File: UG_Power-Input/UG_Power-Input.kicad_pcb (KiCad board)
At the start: 2 copper layers, 45 parts, among them J1 INPUT, J2 OUTPUT, J3 OUTPUT, U1 LM2679

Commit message: Changes to PCB design
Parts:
- added R3: 0Ω, Resistor_THT:R_Axial_DIN0207_L6.3mm_D2.5mm_P10.16mm_Horizontal, F.Cu at (106.9, 109.0)
- H3: footprint MountingHole:MountingHole_3.5mm -> MountingHole:MountingHole_3.5mm_Pad_Via
- R1: value 100kΩ 1% -> 100kΩ
- R2: value 4.99kΩ 1% -> 4.99kΩ; footprint Resistor_THT:R_Axial_DIN0207_L6.3mm_D2.5mm_P2.54mm_Vertical -> Resistor_THT:R_Axial_DIN0207_L6.3mm_D2.5mm_P10.16mm_Horizontal
- moved TP11 65.8 mm to (199.4, 65.3)
- moved F2 65.3 mm to (168.4, 123.7)
- moved TP6 65.0 mm to (181.1, 109.5), turned to 90 degrees
- moved R2 64.5 mm to (190.8, 113.3)
- moved R1 64.5 mm to (172.5, 105.7)
- moved C1 64.5 mm to (167.6, 83.3)
- moved TP10 64.2 mm to (202.7, 86.4)
- moved U1 64.2 mm to (196.1, 108.2)
- moved L1 64.1 mm to (140.7, 79.8)
- moved L3 64.1 mm to (140.7, 113.8)
- moved C7 64.1 mm to (193.3, 108.2)
- moved C9 64.1 mm to (201.2, 105.2)
- moved D1 64.1 mm to (195.6, 103.6)
- moved F1 64.1 mm to (178.3, 69.8)
- moved FL1 64.1 mm to (119.1, 84.3)
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- renumbered TP11 to TP10, TP10 to TP11
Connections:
- net Net-(FL1-Pad2) renamed -IN
- H3 pad 1: (no net) -> Net-(H3-Pad1)
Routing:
- net Net-(H3-Pad1): track 0.00 -> 6.55 mm
- net GND: vias 6 -> 12
- added copper zone on F.Cu, net GND

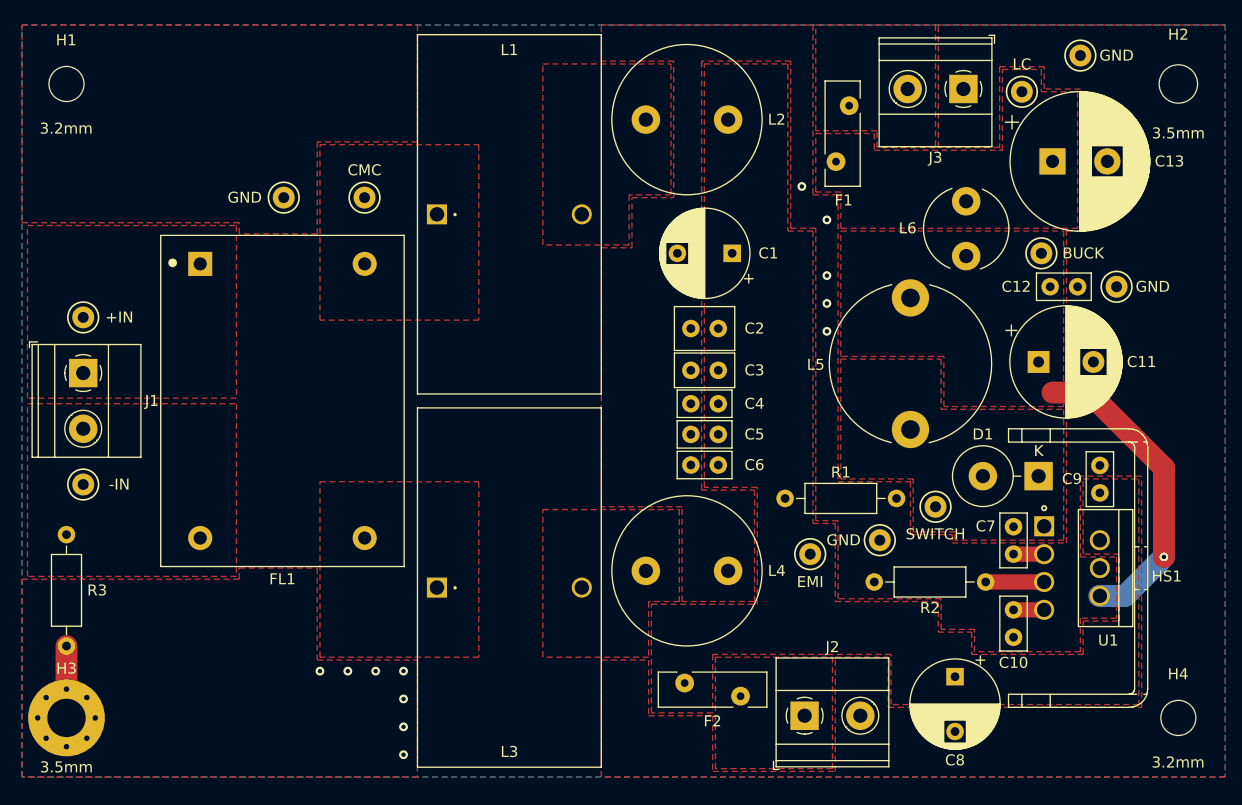
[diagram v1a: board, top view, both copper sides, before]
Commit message: Changes to silkscreen on back of PCB
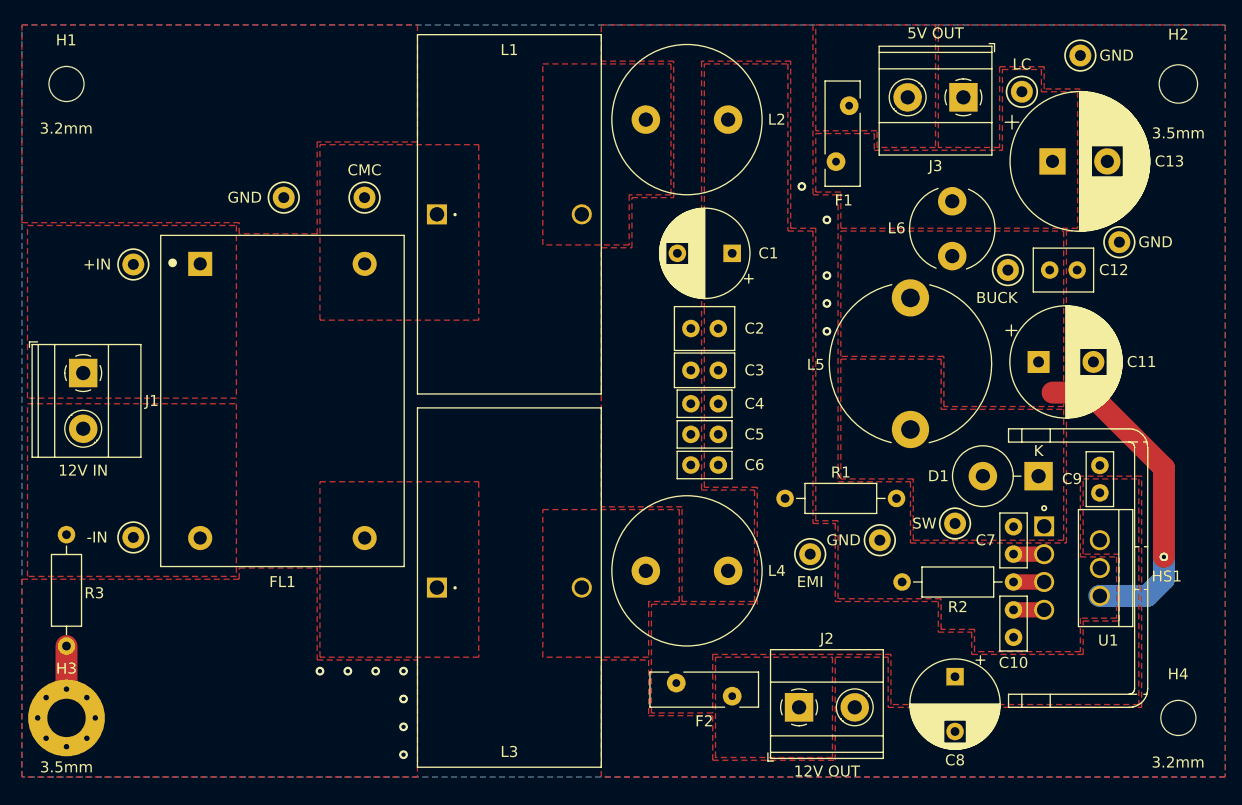
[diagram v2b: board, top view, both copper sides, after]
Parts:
- C12: footprint Capacitor_THT:C_MLCC_W5.0mm_L2.5mm_P2.50mm -> Capacitor_THT:C_MLCC_W5.5mm_L4.0mm_P2.50mm
- J1: value INPUT -> 12V IN
- J2: value OUTPUT -> 12V OUT
- J3: value OUTPUT -> 5V OUT
- TP9: value SWITCH -> SW
- moved TP1 6.65 mm to (113.0, 84.3)
- moved TP4 6.65 mm to (113.0, 109.2)
- moved TP10 4.07 mm to (202.9, 82.3)
- moved TP7 3.41 mm to (192.8, 84.8)
- moved R2 2.54 mm to (193.3, 113.3)
- moved TP9 2.34 mm to (188.0, 108.0)
- moved C12 1.52 mm to (196.6, 84.8)
- moved L6 1.27 mm to (187.7, 83.6)
- moved J2 0.92 mm to (173.7, 124.7)
- moved F2 0.76 mm to (167.6, 123.7)
- moved J3 0.76 mm to (188.7, 69.1)
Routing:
- net Net-(R2-Pad1): track 5.33 -> 2.79 mm
- net BUCK.OUT: track 28.5 -> 29.7 mm

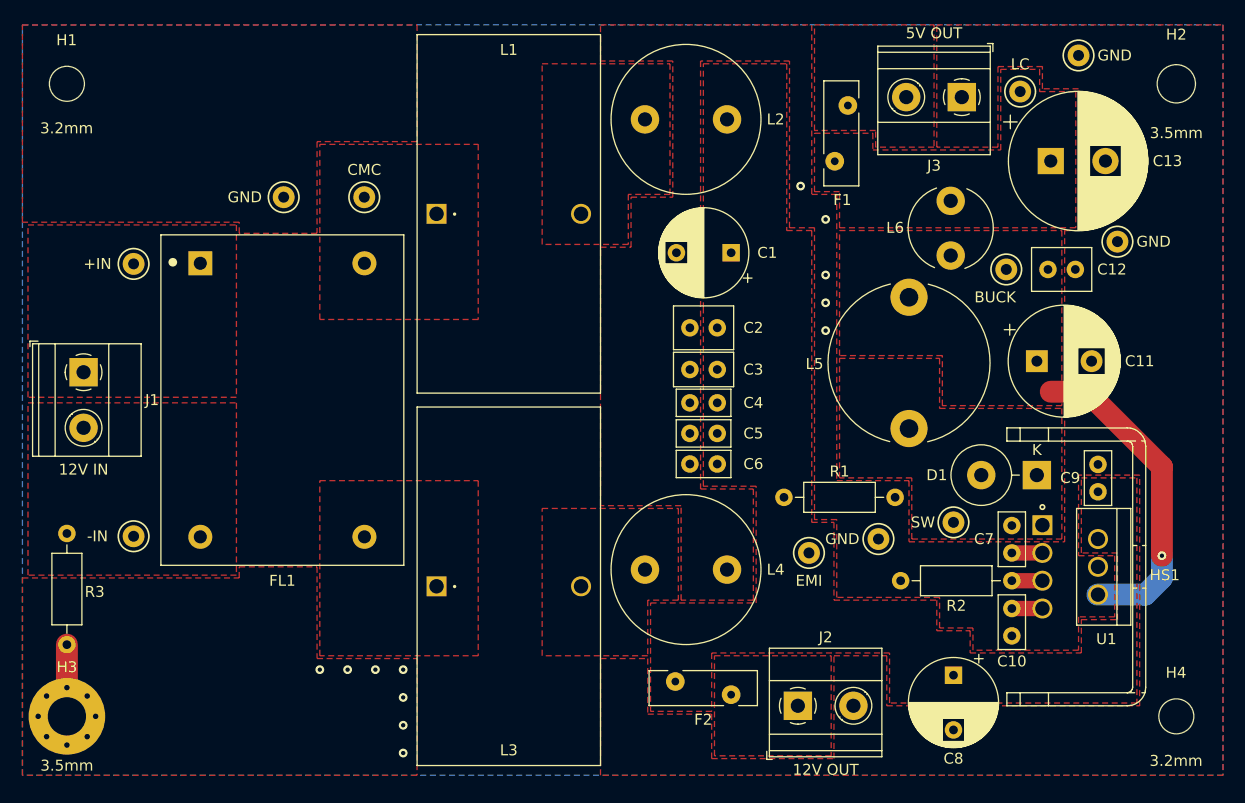
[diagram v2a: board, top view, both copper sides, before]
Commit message: Changes to schematic values, footprints on PCB, BOM
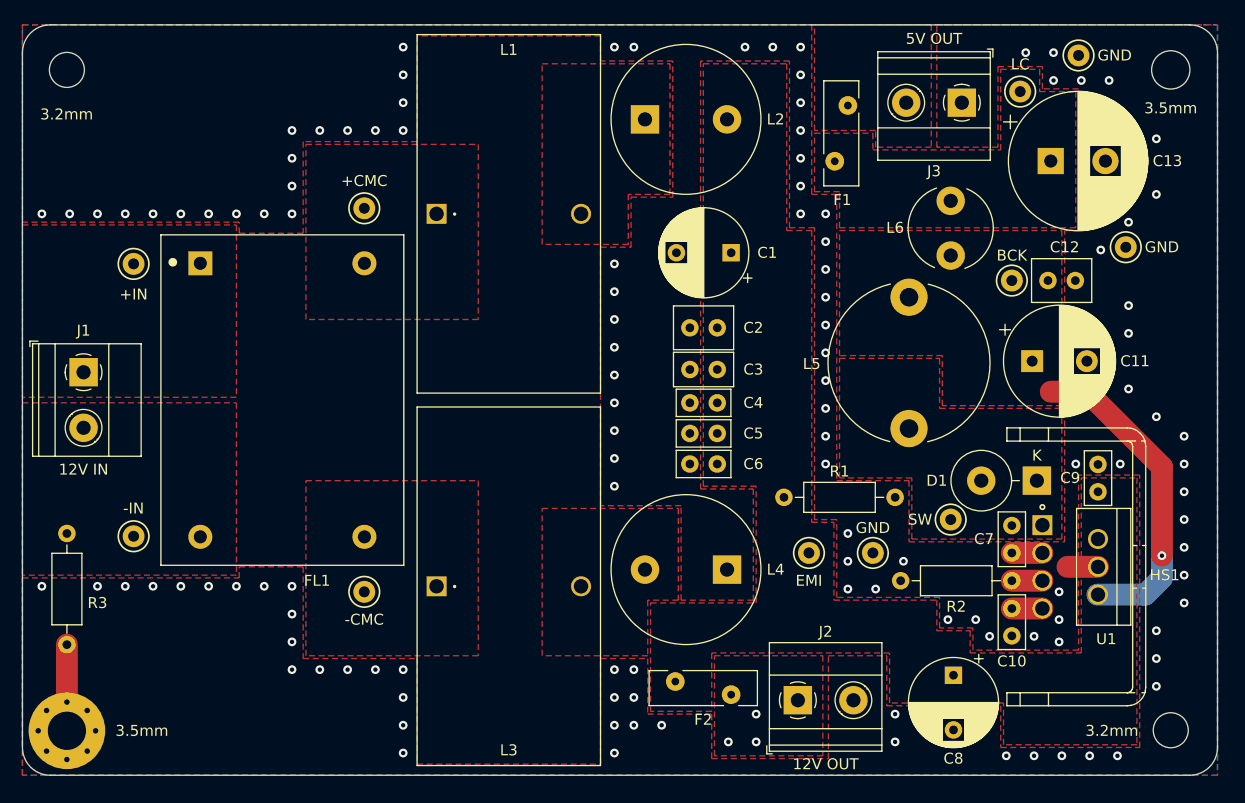
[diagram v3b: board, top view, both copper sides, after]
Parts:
- L5: value 10µH 10A -> 10µH 11.4A
- TP2: value CMC -> +CMC
- TP5: value GND -> -CMC
- TP7: value BUCK -> BCK
- moved TP5 36.8 mm to (134.1, 114.3)
- moved TP6 1.37 mm to (180.6, 110.7)
- moved H2 1.37 mm to (207.8, 66.6)
- moved H4 1.37 mm to (207.8, 126.9)
- moved H3 1.32 mm to (106.9, 127.0)
- moved H1 1.27 mm to (106.9, 66.6)
- moved TP7 1.14 mm to (193.3, 85.9)
- moved C12 1.02 mm to (196.6, 85.9)
- moved TP2 1.02 mm to (134.1, 79.2)
- moved TP10 0.92 mm to (203.7, 82.8)
- moved J3 0.51 mm to (188.7, 69.6)
- moved D1 0.51 mm to (195.6, 104.1)
- moved J2 0.51 mm to (173.7, 124.2)
- moved C11 0.43 mm to (195.2, 93.2)
- moved TP9 0.36 mm to (187.7, 107.7)
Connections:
- TP5 pad 1: GND -> Net-(FL1-Pad3)
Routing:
- net GND: track 0.00 -> 2.79 mm, vias 12 -> 124
- net Net-(H3-Pad1): track 6.55 -> 7.82 mm
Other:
- board outline added: 109.2 x 68.6 mm

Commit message: Changes to PCB & BOM
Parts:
- moved F1 12.0 mm to (190.2, 70.6)
- moved L6 5.33 mm to (182.4, 83.6)
- moved J3 5.08 mm to (183.6, 69.6)
- moved TP7 0.25 mm to (193.0, 85.9)
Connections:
- J3 pad 1: GND -> Net-(F1-Pad1)
- J3 pad 2: Net-(F1-Pad1) -> GND
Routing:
- net GND: vias 124 -> 121

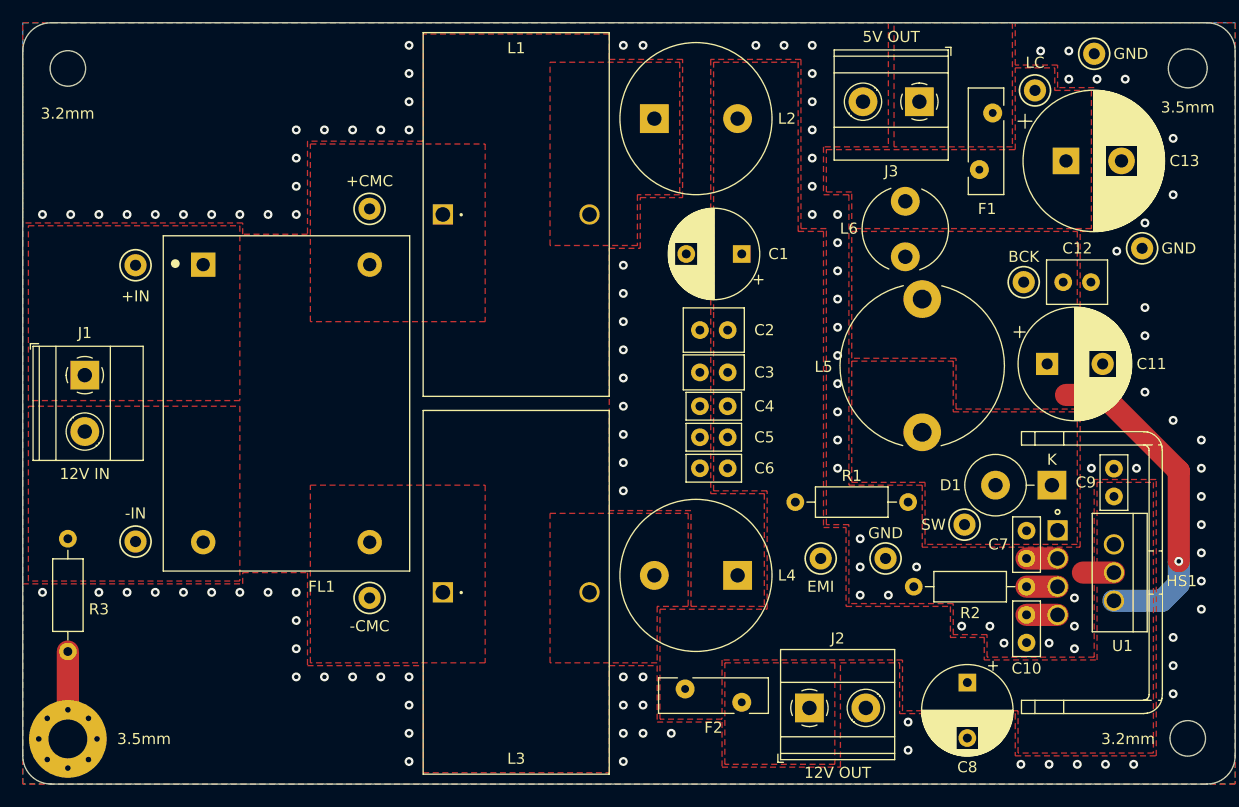
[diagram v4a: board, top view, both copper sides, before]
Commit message: Silkscreen fixes
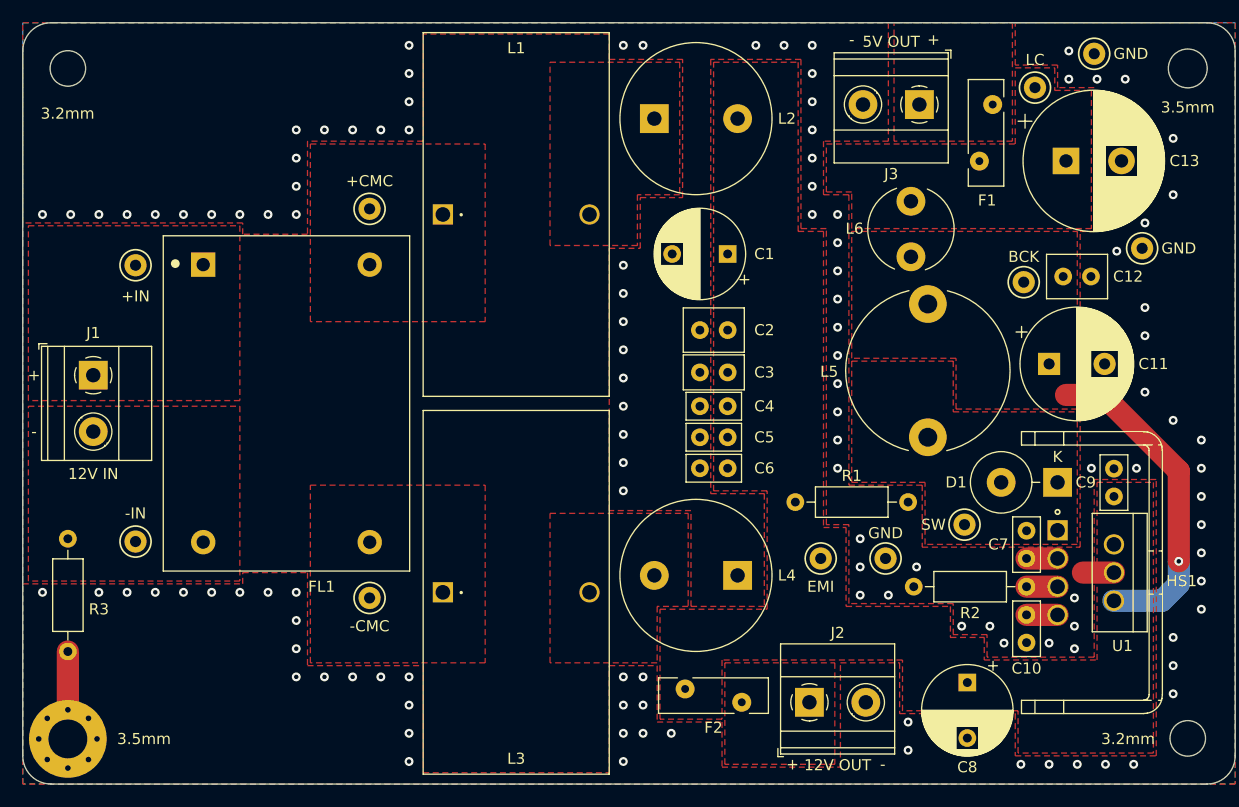
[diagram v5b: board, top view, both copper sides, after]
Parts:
- moved C1 1.27 mm to (166.4, 83.3)
- moved J1 0.76 mm to (109.2, 94.2)
- moved F1 0.76 mm to (190.2, 69.8)
- moved L5 0.68 mm to (184.4, 99.8)
- moved D1 0.57 mm to (196.1, 103.9)
- moved C12 0.51 mm to (196.6, 85.3)
- moved J2 0.51 mm to (173.7, 123.7)
- moved L6 0.51 mm to (182.9, 83.6)
- moved TP8 0.25 mm to (194.1, 68.3)
- moved J3 0.25 mm to (183.6, 69.8)
- moved C11 0.17 mm to (195.3, 93.2)
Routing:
- net GND: vias 121 -> 120
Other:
- board text added: "+"
- board text added: "-"
